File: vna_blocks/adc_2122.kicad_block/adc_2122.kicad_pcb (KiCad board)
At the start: 4 copper layers, 34 parts, among them U15 LTC2122IUK-TRPBF

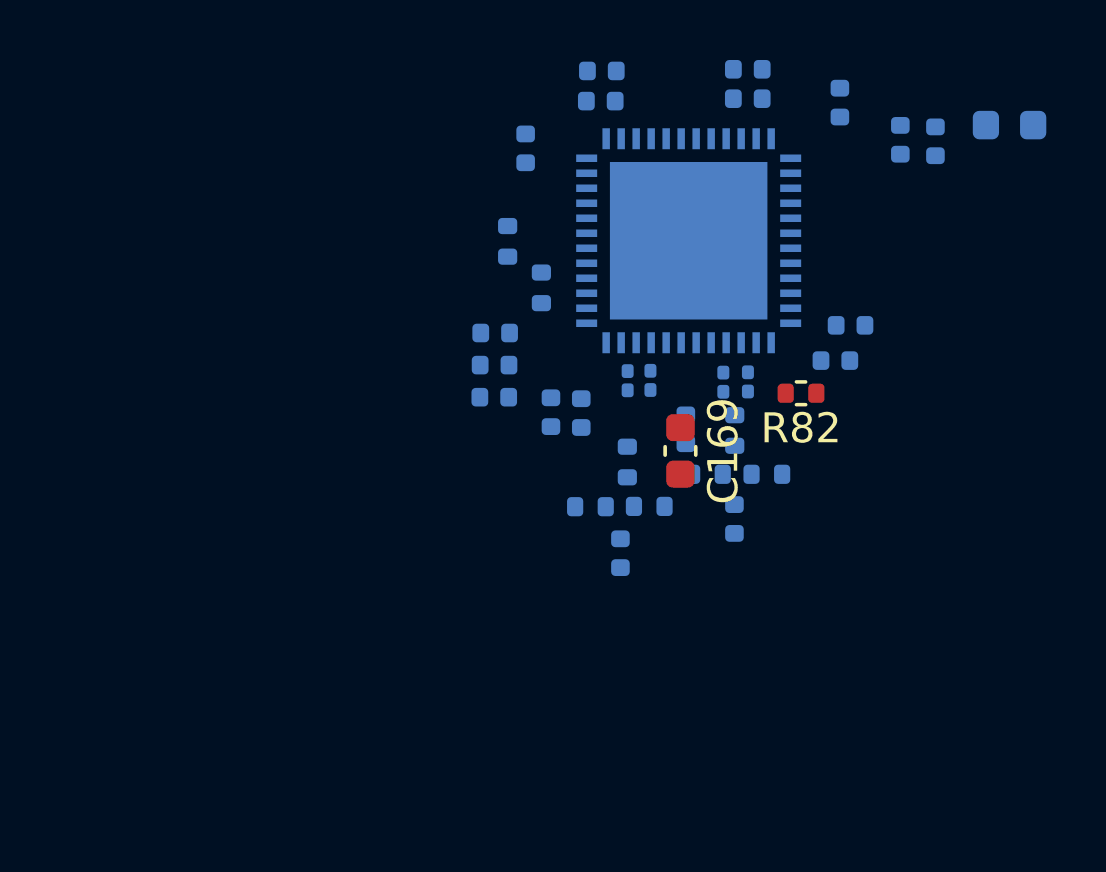
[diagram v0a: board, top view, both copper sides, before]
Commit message: fixed 50 ohm for coax port, fixed power blocks
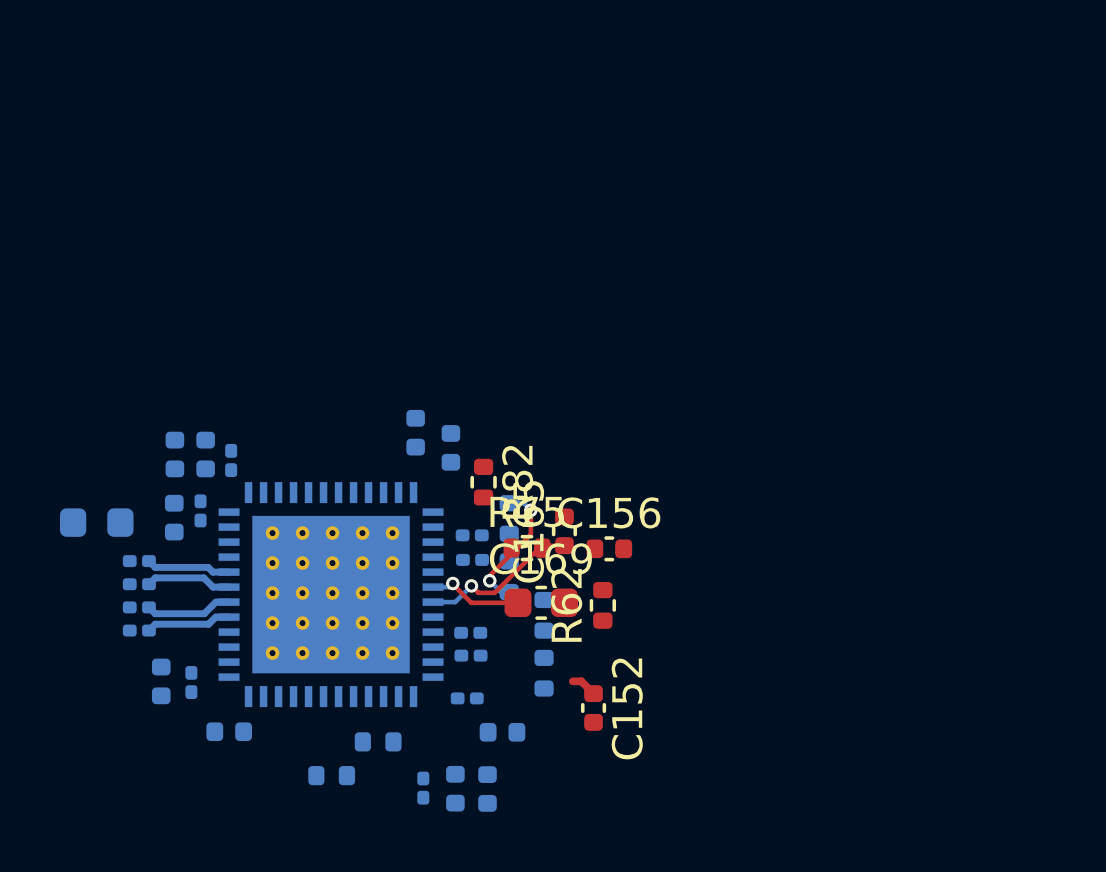
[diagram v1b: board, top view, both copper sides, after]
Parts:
- added C256: 0.1u, Capacitor_SMD:C_0201_0603Metric, B.Cu at (203.5, 118.7)
- added C257: 0.1u, Capacitor_SMD:C_0201_0603Metric, B.Cu at (203.5, 119.5)
- added C262: 0.1u, Capacitor_SMD:C_0201_0603Metric, B.Cu at (203.5, 120.2)
- added C266: 0.1u, Capacitor_SMD:C_0201_0603Metric, B.Cu at (203.5, 121.0)
- C150, C180, C414, C417, C418: footprint Capacitor_SMD:C_0402_1005Metric -> Capacitor_SMD:C_0201_0603Metric
- C152, C156, C165, R62, R75: moved to F.Cu
- moved FB3 33.2 mm to (202.1, 117.4), turned to 0 degrees
- moved C144 27.4 mm to (204.7, 115.2), turned to 90 degrees
- moved C146 25.4 mm to (205.7, 115.2), turned to 90 degrees
- moved C175 25.1 mm to (204.2, 122.7), turned to -90 degrees
- moved C176 24.3 mm to (204.7, 117.3), turned to -90 degrees
- moved C418 23.7 mm to (205.2, 122.8), turned to -90 degrees
- moved C150 23.5 mm to (206.5, 115.3)
- moved C414 22.8 mm to (205.5, 117.0), turned to -90 degrees
- moved C177 21.8 mm to (206.5, 124.4), turned to 0 degrees
- moved R65 18.8 mm to (209.9, 125.9), turned to 180 degrees
- moved U15 16.8 mm to (209.9, 119.8), turned to 180 degrees
- moved R74 16.1 mm to (211.4, 124.7), turned to 180 degrees
- moved C180 15.4 mm to (213.0, 126.3), turned to -90 degrees
- moved C171 14.9 mm to (212.7, 114.4), turned to 90 degrees
- moved C164 14.2 mm to (214.0, 126.3), turned to 90 degrees
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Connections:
- net /1V8D renamed /1V8_IO
- C165 pad 1: /Detector_adc_stage/V_CM -> /Detector_adc_stage/V_CM1
- R72 pad 1: /RCVR1_IFR_P -> /RCVR1_IFR_N
- R73 pad 2: /RCVR1_IFR_N -> /RCVR1_IFR_P
- R80 pad 1: /RCVR1_IFR_P -> /RCVR1_IFR_N
- R81 pad 1: /RCVR1_IFR_N -> /RCVR1_IFR_P
- U15 pad 29: DAT_B_N -> /Detector_adc_stage/B-
- U15 pad 30: DAT_B_P -> /Detector_adc_stage/B+
- U15 pad 31: DAT_A_N -> /Detector_adc_stage/A-
- U15 pad 32: DAT_A_P -> /Detector_adc_stage/A+
- U15 pad 7: /Detector_adc_stage/V_CM -> /Detector_adc_stage/V_CM1
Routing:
- net /Detector_adc_stage/V_CM1: track 0.00 -> 5.41 mm, vias 0 -> 1
- net Net-(C156-Pad1): track 0.00 -> 4.54 mm, vias 0 -> 2
- net Net-(U15-VREF): track 0.14 -> 3.31 mm, vias 0 -> 1
- net /Detector_adc_stage/B+: track 0.00 -> 2.92 mm
- net /Detector_adc_stage/A-: track 0.00 -> 2.88 mm
- net /Detector_adc_stage/B-: track 0.00 -> 2.86 mm
- net /Detector_adc_stage/A+: track 0.00 -> 2.82 mm
- net Net-(C152-Pad1): track 0.00 -> 0.86 mm
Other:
- copper layers 4 -> 8
